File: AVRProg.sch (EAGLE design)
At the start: 23 parts, among them IC2 LD111733, IC3 ATMEGA8, J1 Program, J2 Slow Clock, J3 USB, J4 ISP Target, J5 VDD Select, Q1 12 MHz

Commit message: foo
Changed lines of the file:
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@@
 </instance>
 <instance part="LED1" gate="G$1" x="60.96" y="127" smashed="yes" rot="R180">
-<attribute name="NAME" x="50.8" y="140.208" size="1.27" layer="95"/>
-<attribute name="VALUE" x="50.8" y="142.24" size="1.27" layer="96"/>
+<attribute name="NAME" x="50.8" y="141.986" size="1.27" layer="95"/>
+<attribute name="VALUE" x="50.8" y="140.208" size="1.27" layer="96"/>
 </instance>
 <instance part="R2" gate="C" x="76.2" y="119.38" smashed="yes" rot="MR0">

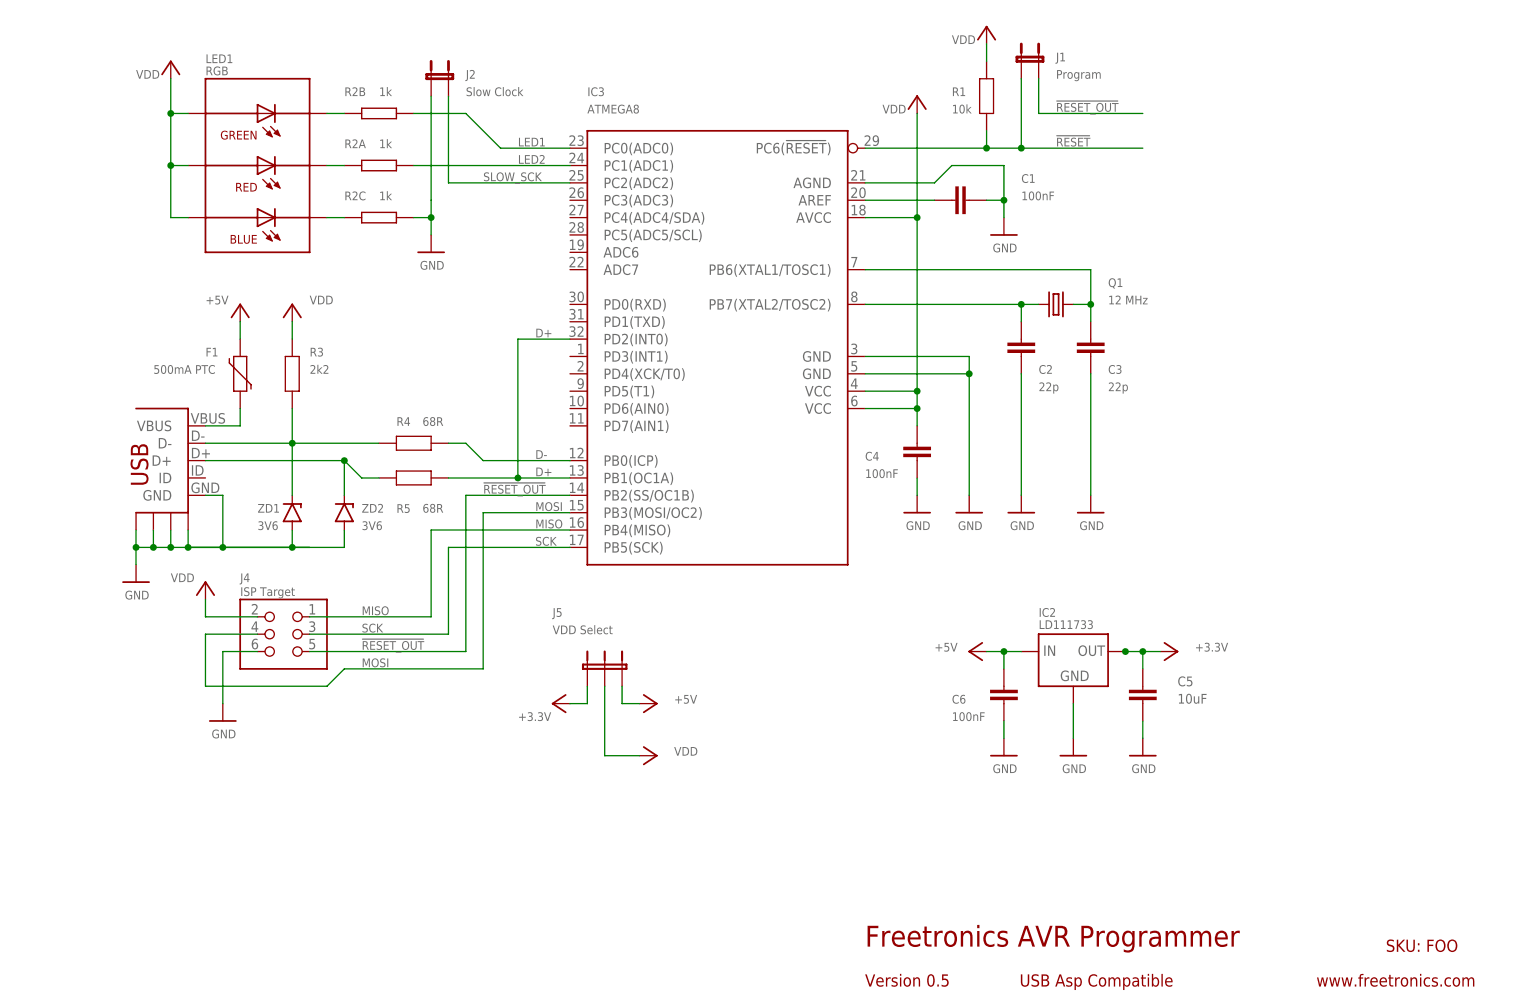
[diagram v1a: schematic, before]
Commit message: changed zeners to miniMELF, moved jumpers to increase clearance around ISP header, added 10uF cap on 5V rail.
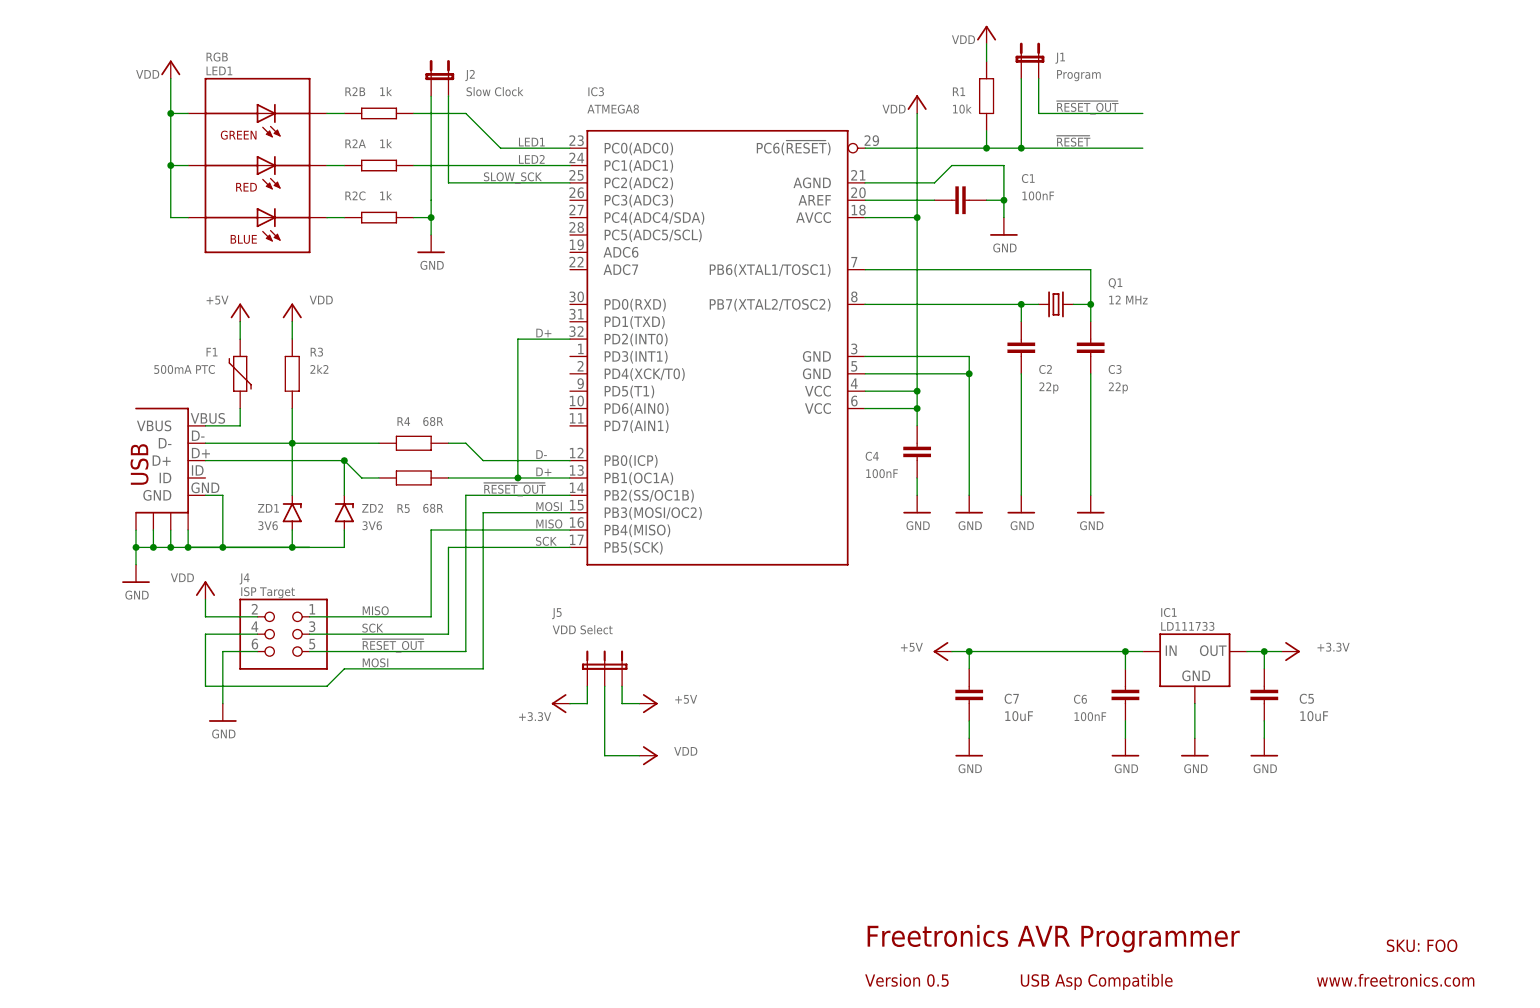
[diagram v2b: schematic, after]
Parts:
- removed IC2: LD111733, freetronics-luke:LD1117-FIXED
- added C7: 10uF, freetronics-jon:C-EUC0805
- added IC1: LD111733, freetronics-luke:LD1117-FIXED
- ZD1, ZD2: device freetronics-luke:ZENER -> freetronics-luke:ZENERMINIMELF
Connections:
- net +3V3: now also IC1.OUT; no longer IC2.OUT, IC2.OUT@1
- net +5V: now also C7.1, IC1.IN; no longer IC2.IN
- net GND: now also C7.2, IC1.GND; no longer IC2.GND
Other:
- note added: "MINI MELF"
- note added: "ZD1, ZD2: 3.6V 500mW Zener, glass MINIMELF packages, eg. BZV55C3V6"
- note removed: "SOD-323"
- note removed: "ZD1, ZD2: 3.6V 200mW Zener, SOD-323 packages, eg. MM3Z3V6T1G"
- moved on the sheet: C5, C6

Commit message: foo
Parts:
- removed IC3: ATMEGA8, freetronics-luke:ATMEGA168
- added C8: 100nF, freetronics-master-v1:CAP0603
- added IC2: LD111733, freetronics-luke:LD1117-FIXED
- C4, C6: value 100nF -> 10uF; device freetronics-master-v1:CAP0603 -> freetronics-jon:C-EUC0805
- C5: value 10uF -> 100nF; device freetronics-jon:C-EUC0805 -> freetronics-master-v1:CAP0603
- IC1: value LD111733 -> ATMEGA8; device freetronics-luke:LD1117-FIXED -> freetronics-luke:ATMEGA168
- J2: value Slow Clock -> Slow clock
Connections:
- net !RESET: now also IC1.PC6(!RESET!), J1.1; no longer IC3.PC6(!RESET!), J1.2
- net !RESET_OUT: now also IC1.PB2(SS/OC1B), J1.2; no longer IC3.PB2(SS/OC1B), J1.1
- net +3V3: now also C7.1, IC2.OUT; no longer C5.1, IC1.OUT
- net +5V: now also C8.1, IC2.IN; no longer C7.1, IC1.IN
- net D+: now also IC1.PB1(OC1A), IC1.PD2(INT0); no longer IC3.PB1(OC1A), IC3.PD2(INT0)
- net D-: now also IC1.PB0(ICP); no longer IC3.PB0(ICP)
- net GND: now also C8.2, IC1.AGND, IC1.GND@1, IC1.GND@2, IC2.GND, J2.1; no longer IC1.GND, IC3.AGND, IC3.GND@1, IC3.GND@2, J2.2
- net LED1: now also IC1.PC0(ADC0); no longer IC3.PC0(ADC0)
- net LED2: now also IC1.PC1(ADC1); no longer IC3.PC1(ADC1)
- net MISO: now also IC1.PB4(MISO); no longer IC3.PB4(MISO)
- net MOSI: now also IC1.PB3(MOSI/OC2); no longer IC3.PB3(MOSI/OC2)
- net N$138: now also IC1.PB6(XTAL1/TOSC1); no longer IC3.PB6(XTAL1/TOSC1)
- net N$139: now also IC1.PB7(XTAL2/TOSC2); no longer IC3.PB7(XTAL2/TOSC2)
- net N$142: now also IC1.AREF; no longer IC3.AREF
- net SCK: now also IC1.PB5(SCK); no longer IC3.PB5(SCK)
- net SLOW_SCK: now also IC1.PC2(ADC2), J2.2; no longer IC3.PC2(ADC2), J2.1
- net VDD: now also C5.1, IC1.AVCC, IC1.VCC@1, IC1.VCC@2; no longer IC3.AVCC, IC3.VCC@1, IC3.VCC@2
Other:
- note added: "0805"
- note added: "Blue: Power"
- note added: "Green: Active"
- note added: "Red: Write"
- note added: "SKU: AVRPROG"
- note removed: "SKU: FOO"
- moved on the sheet: C2, C3, C4, C5, C6, C7, J5, Q1

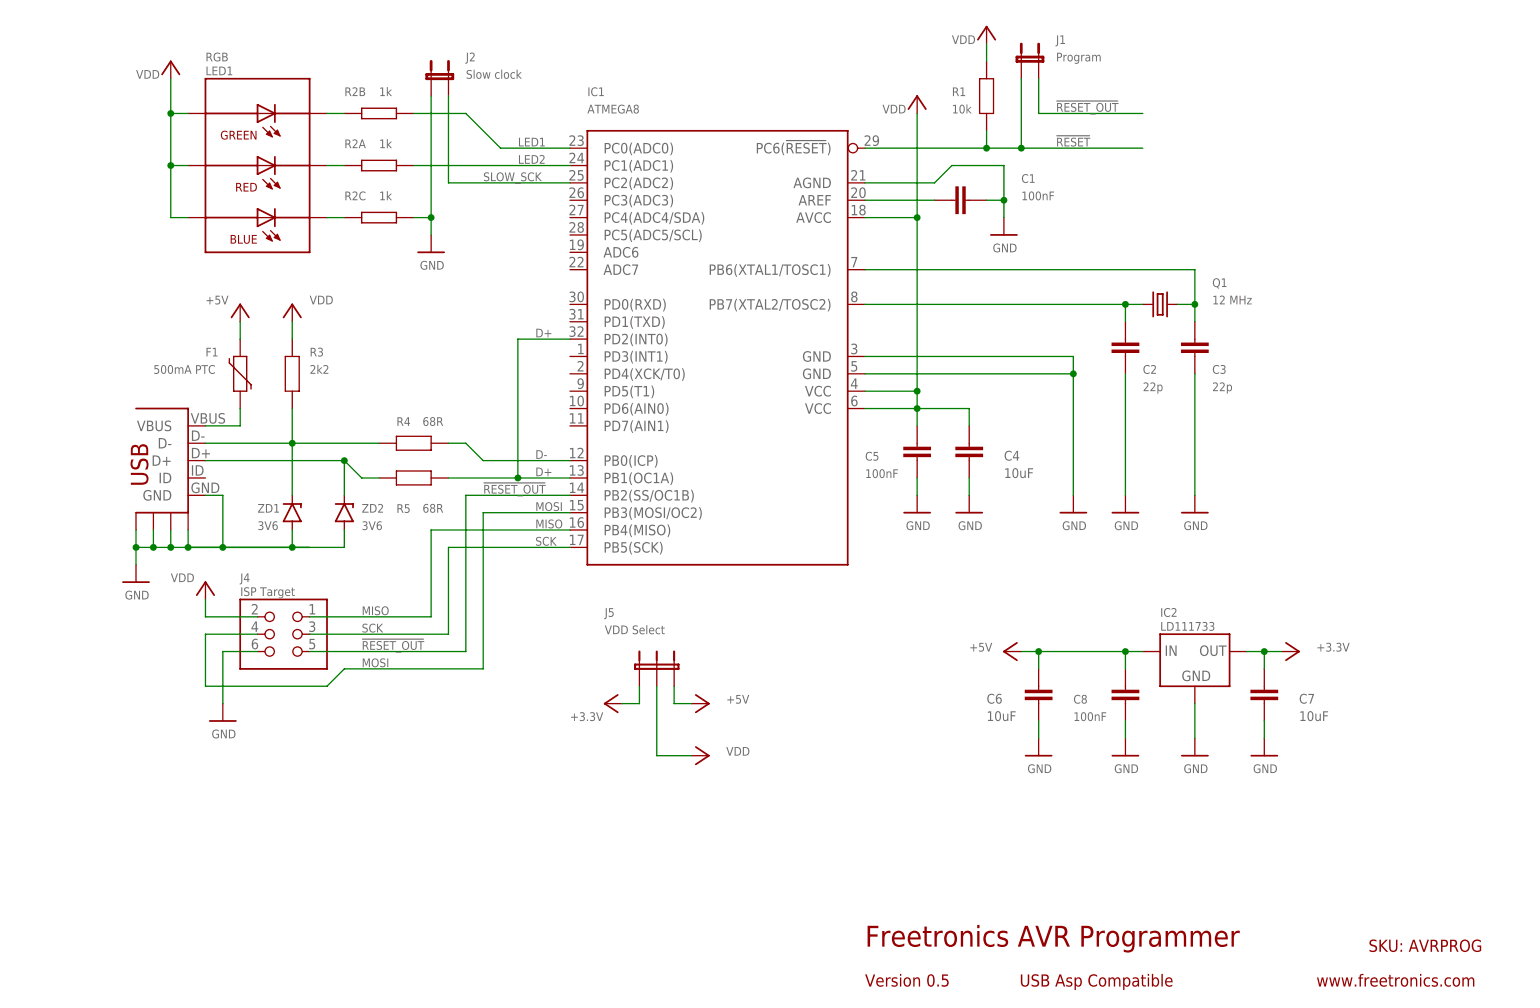
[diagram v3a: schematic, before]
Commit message: Schematic and layout improvements
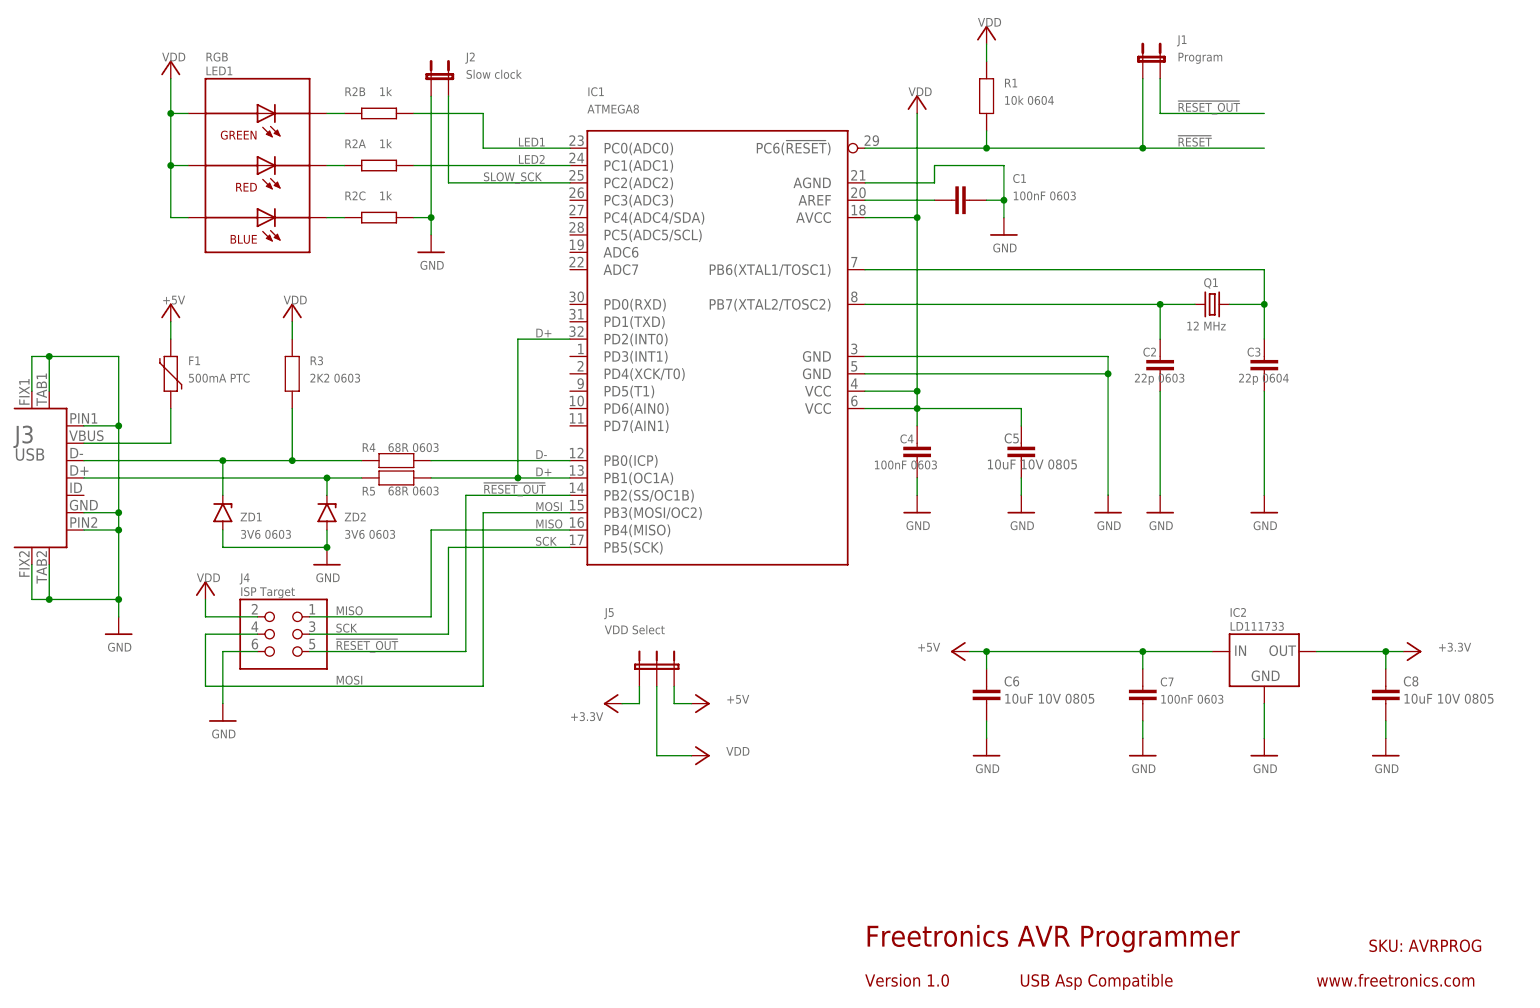
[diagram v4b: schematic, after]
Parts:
- C1: value 100nF -> 100nF 0603
- C2: value 22p -> 22p 0603
- C3: value 22p -> 22p 0604
- C4, C7: value 10uF -> 100nF 0603; device freetronics-jon:C-EUC0805 -> freetronics-master-v1:CAP0603
- C5, C8: value 100nF -> 10uF 10V 0805; device freetronics-master-v1:CAP0603 -> freetronics-jon:C-EUC0805
- C6: value 10uF -> 10uF 10V 0805
- J3: device freetronics-luke:USB-FT -> freetronics-jon:USB-6PSMT
- R1: value 10k -> 10k 0604
- R3: value 2k2 -> 2K2 0603
- R4, R5: value 68R -> 68R 0603
- ZD1, ZD2: value 3V6 -> 3V6 0603
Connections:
- net +3V3: now also C8.1; no longer C7.1
- net +5V: now also C7.1; no longer C8.1
- net GND: now also J3.FIX1, J3.FIX2, J3.PIN1, J3.PIN2, J3.TAB1, J3.TAB2; no longer J3.SH$1, J3.SH$2, J3.SH$3, J3.SH$4
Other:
- note added: "J1, J2: 2-pin 0.1" through-hole pin headers (not placed)"
- note added: "Version 1.0"
- note removed: "0603"
- note removed: "0805"
- note removed: "0805 ceramic"
- note removed: "10V"
- note removed: "J1, J2: 2-pin 0.1" through-hole pin headers"
- note removed: "Version 0.5"
- moved on the sheet: C2, C3, C4, C5, C6, C7, C8, F1, IC2, J1, Q1, R4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
